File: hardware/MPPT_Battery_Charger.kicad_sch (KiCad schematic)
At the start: 74 parts, among them Q24 SI7414DN-T1-E3, Q25 SI7414DN-T1-E3, Q5 SI7414DN-T1-E3, Q6 SI7414DN-T1-E3, Q8 SI2302DDS-T1-GE3, U22 BQ24650RVAT, U26 LMV321RIYLT, U28 LMV321RIYLT, U4 INA199C1DCKR

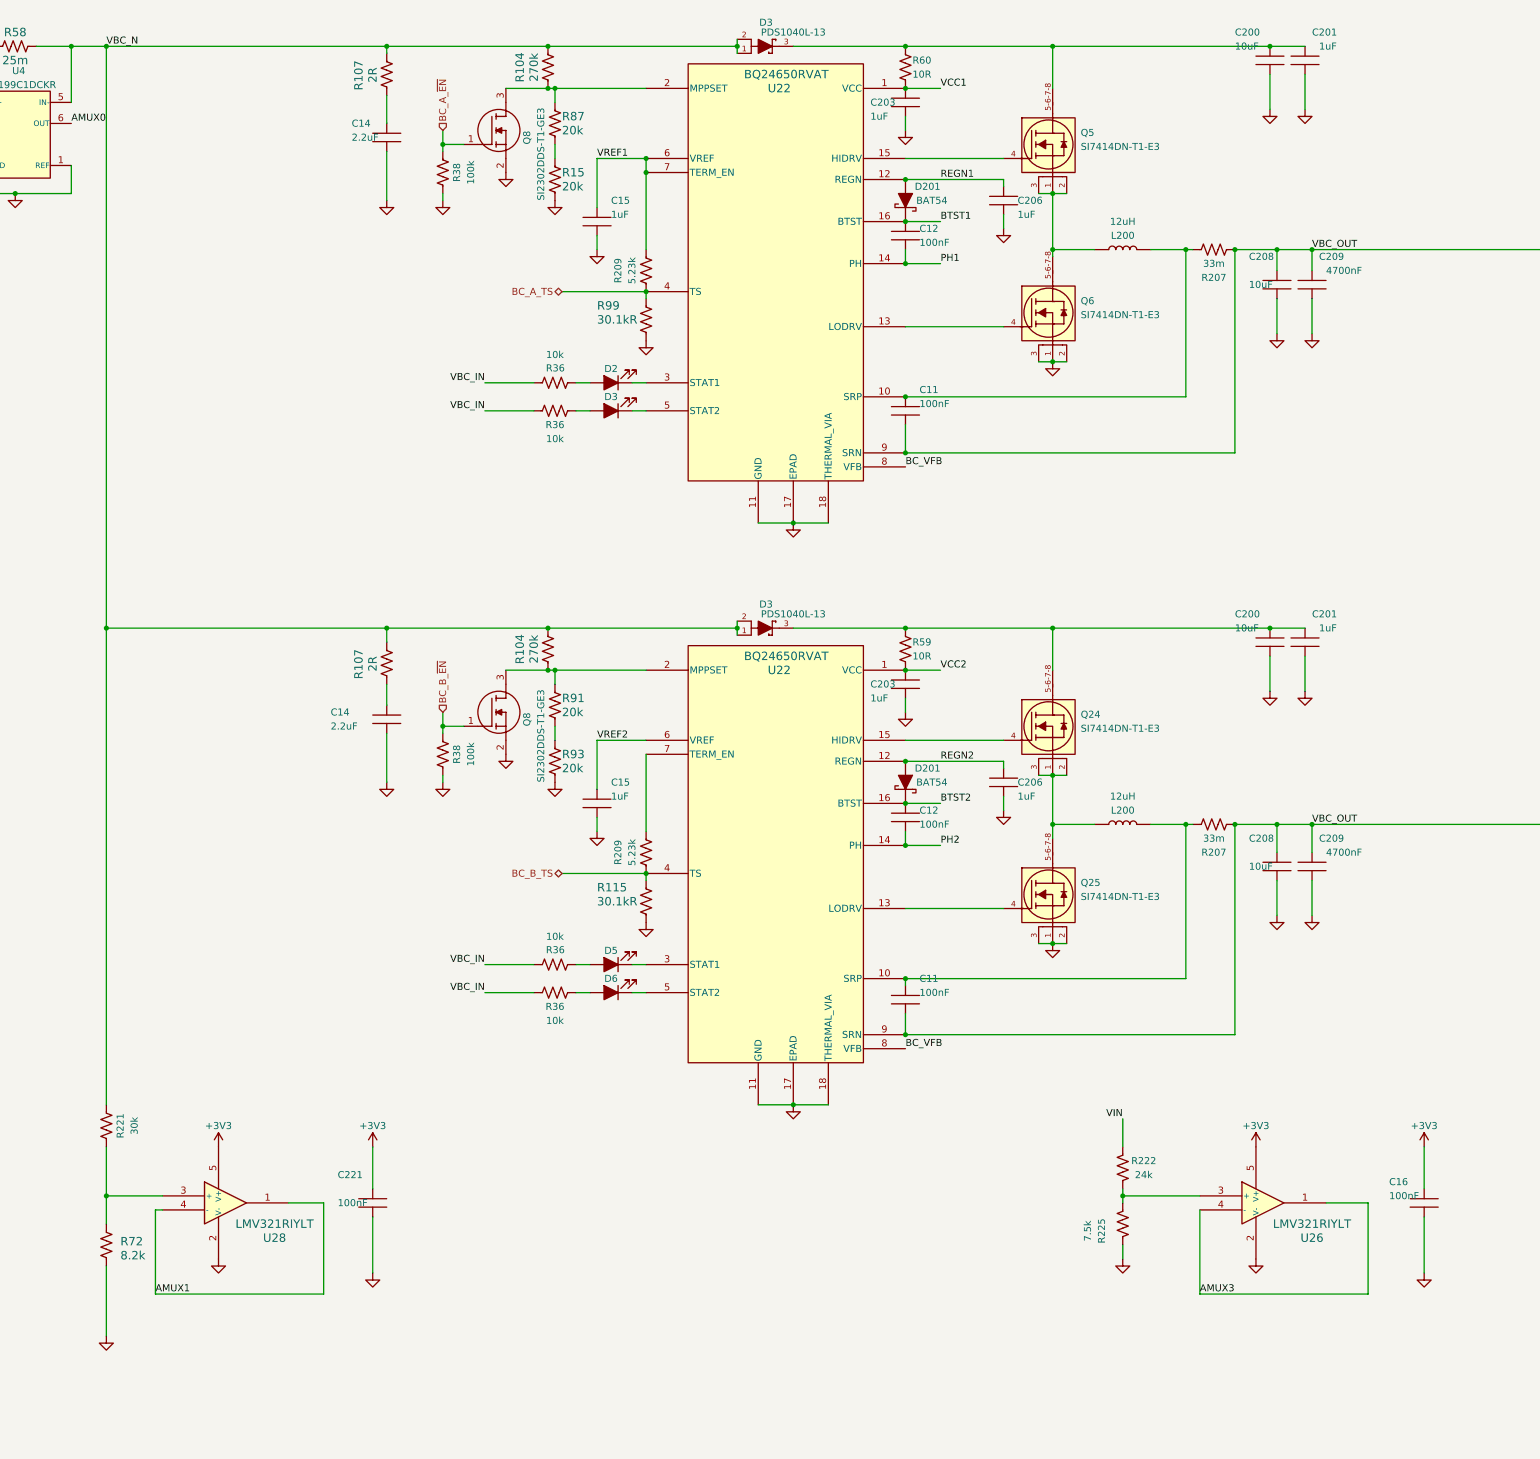
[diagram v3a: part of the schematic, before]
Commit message: hardware: Updating the schematic considering issues #2, #3, #4, #5 and #6.
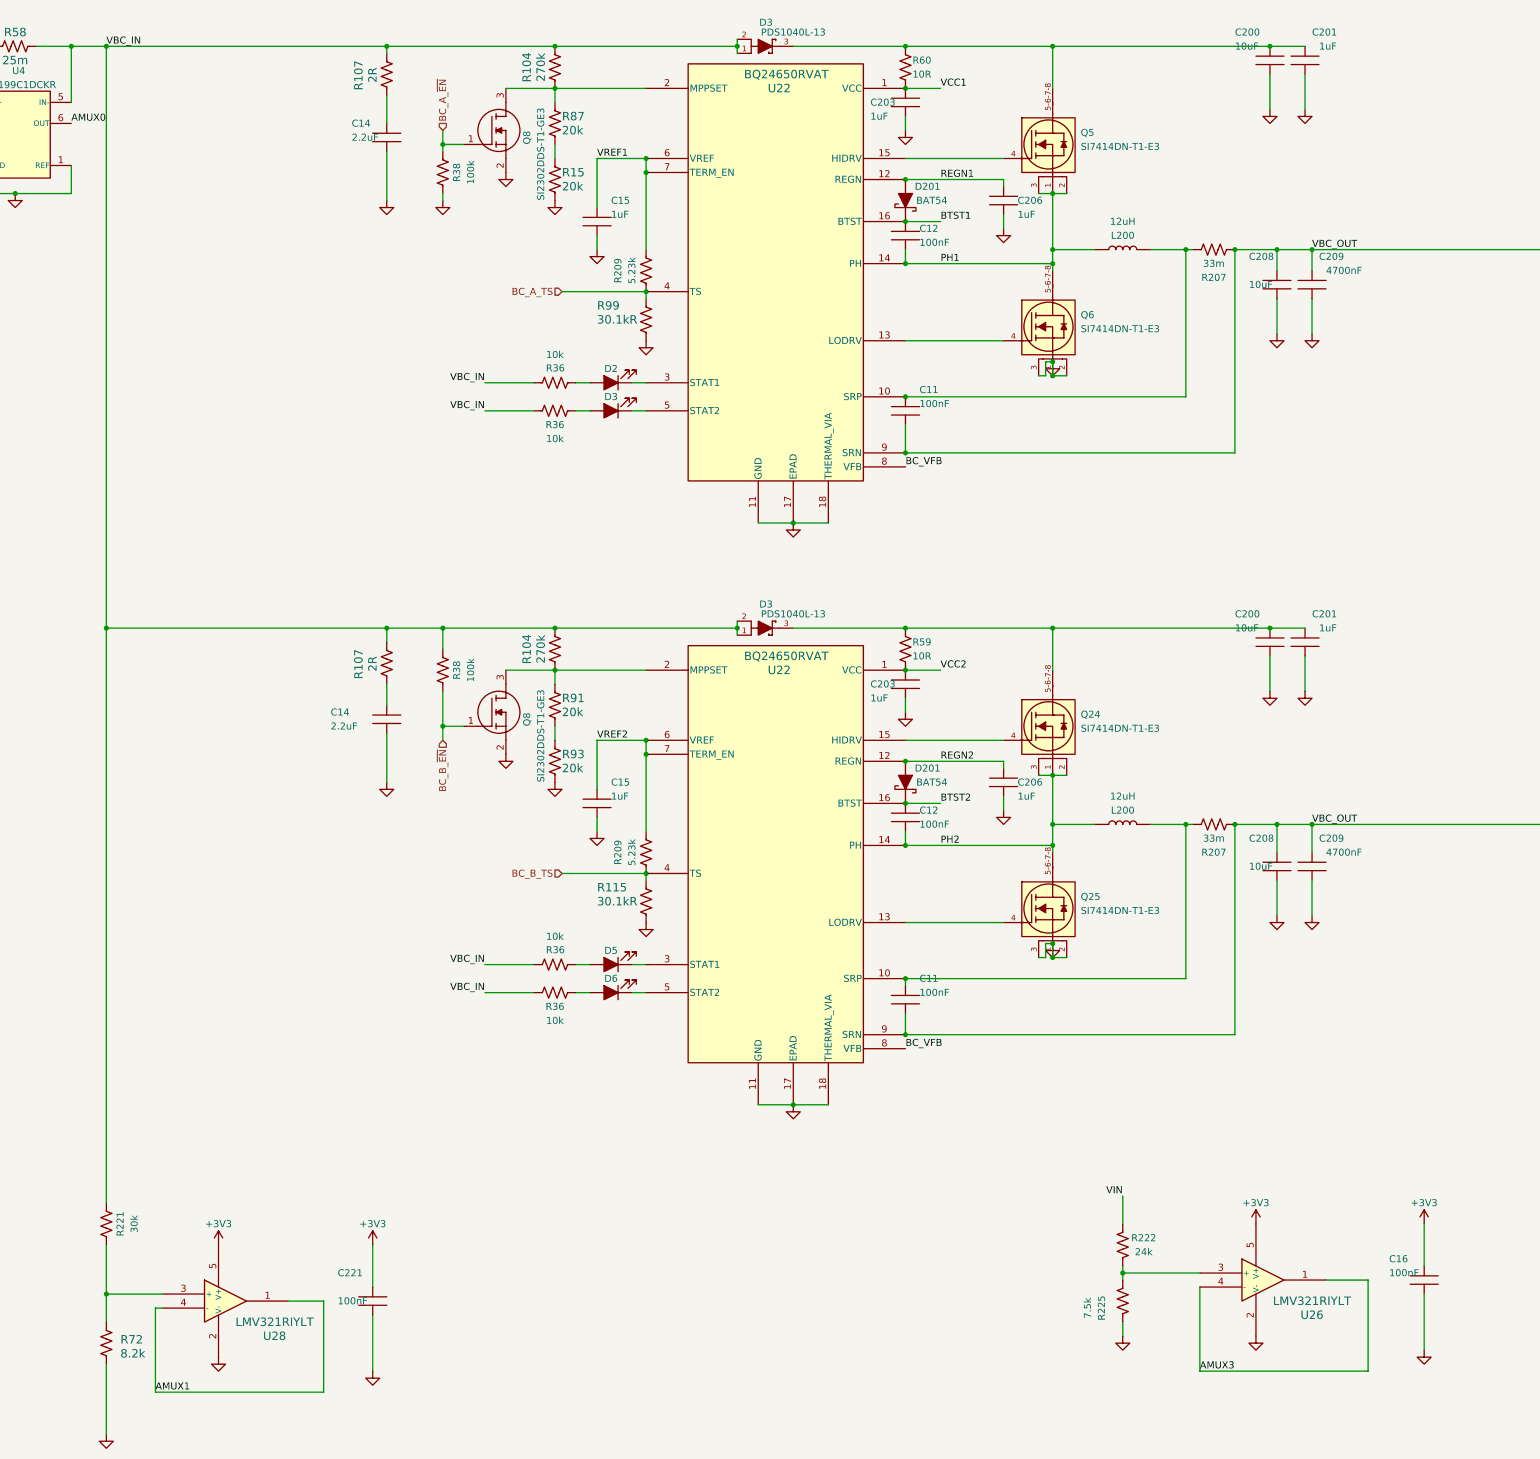
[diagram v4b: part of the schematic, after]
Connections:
- net VBC_N is gone; now on net VBC_IN: D3.1, D3.1, D3.2, D3.2, R104.2, R104.2, R107.2, R107.2, R221.2, R58.1, U4.5 (IN-)
- net BC_B_~{EN}: now also R38.1; no longer R38.2
- net GND: no longer R38.1
- net PH1: now also L200.1, Q5.1 (S), Q5.2 (S), Q5.3 (S), Q6.5-6-7-8 (D)
- net PH2: now also L200.1, Q24.1 (S), Q24.2 (S), Q24.3 (S), Q25.5-6-7-8 (D)
- net VBC_IN: now also R38.2
- net VREF2: now also R209.2, U22.7 (TERM_EN)
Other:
- moved on the sheet: C16, C221, Q25, Q6, R104, R221, R222, R225, R38, R72, U26, U28

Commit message: hardware: Updating 3D models, component placement and more.
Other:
- title: (none) -> Reliability Enhanced Electrical Power System
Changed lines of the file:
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@@
 (kicad_sch (version 20230121) (generator eeschema)
   (paper "A3")
+  (title_block
+    (title "Reliability Enhanced Electrical Power System")
+    (date "2023-08-03")
+    (rev "v0.0")
+    (comment 1 "João C. E. Barcellos <joaoclaudiobarcellos@gmail.com>")
+    (comment 2 "Laura Debastiani <laudebastiani@gmail.com>")
+  )
   (junction (at 196.85 137.16) (diameter 0) (color 0 0 0 0)
   )

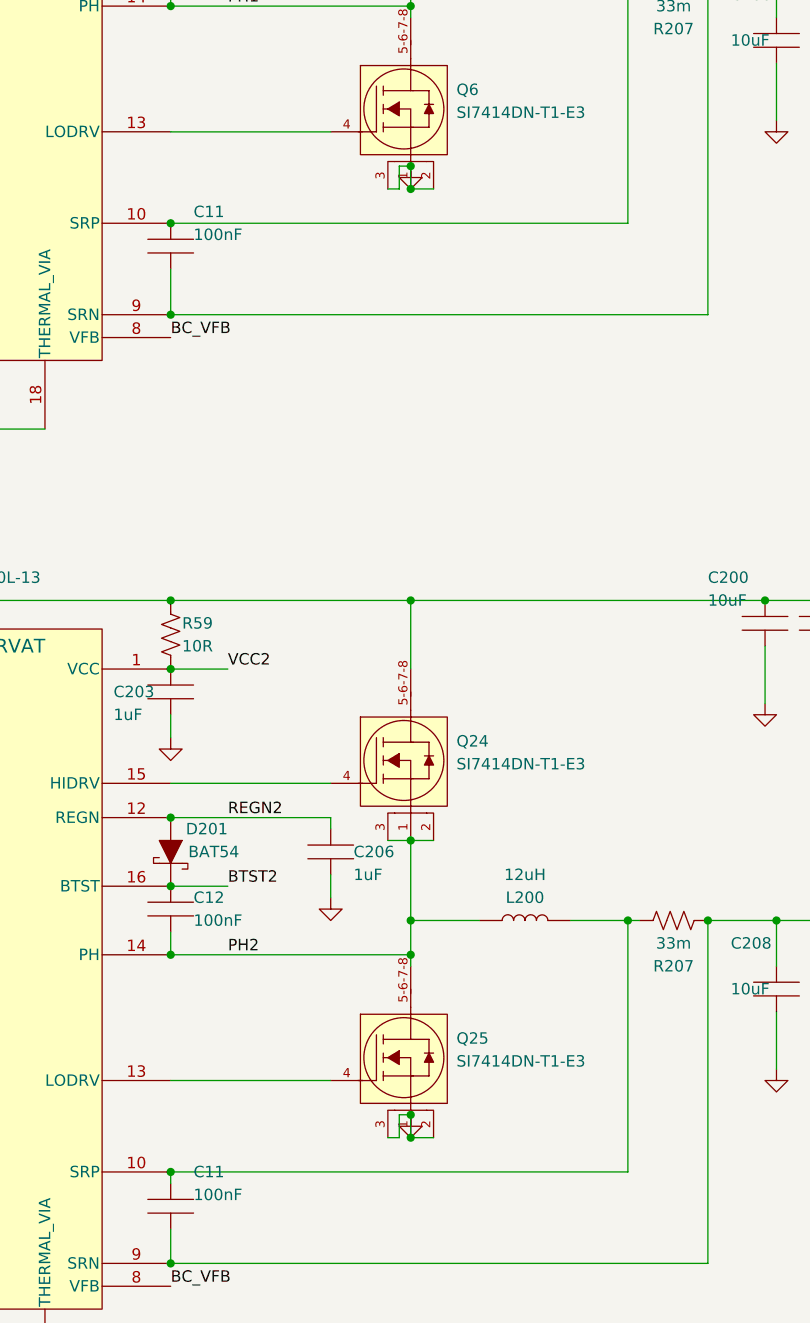
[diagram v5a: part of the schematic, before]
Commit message: hardware: Adding some 3D models, changing the placement of components and routing more nets.
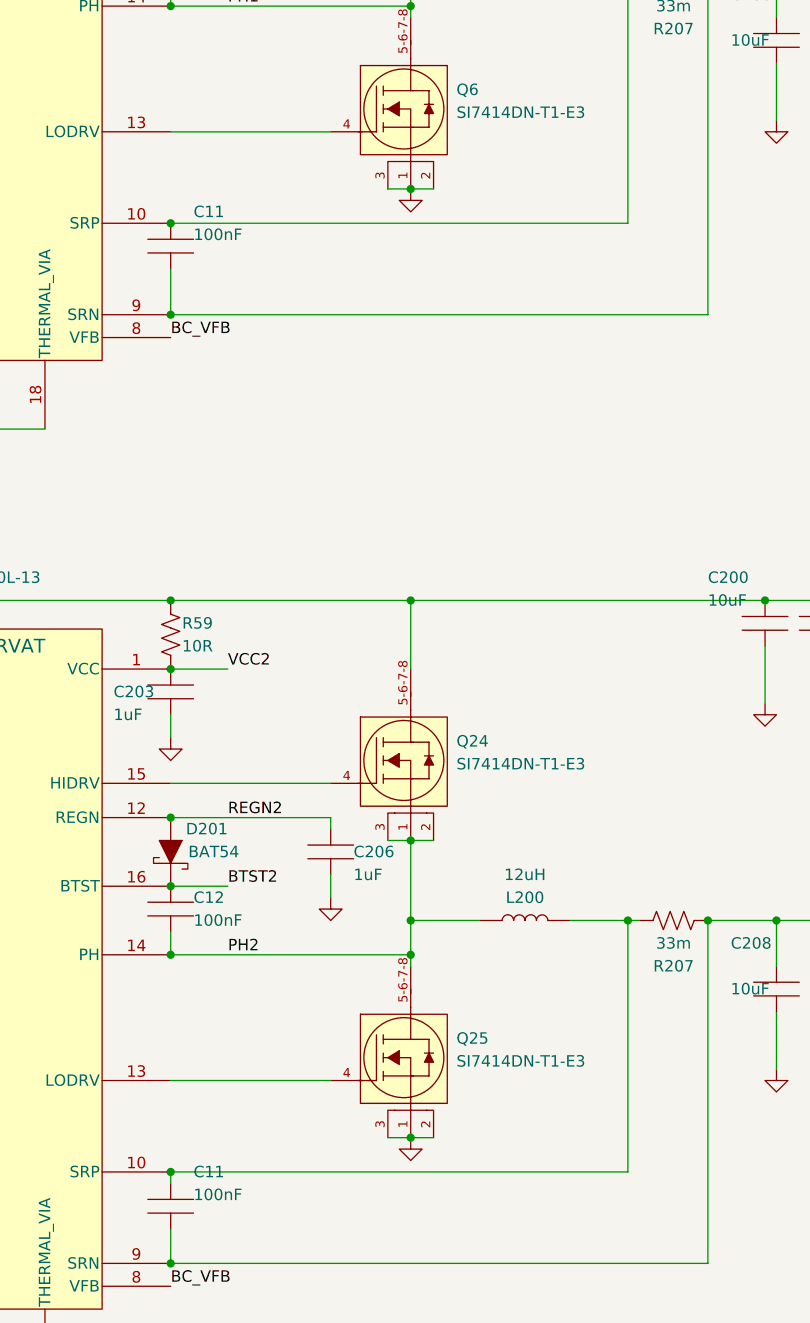
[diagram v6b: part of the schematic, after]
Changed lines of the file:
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@@
   (junction (at 196.85 129.54) (diameter 0) (color 0 0 0 0)
   )
+  (junction (at 223.52 189.23) (diameter 0) (color 0 0 0 0)
+  )
   (junction (at 369.57 87.63) (diameter 0) (color 0 0 0 0)
   )
@@
   (junction (at 45.72 24.13) (diameter 0) (color 0 0 0 0)
   )
-  (junction (at 223.52 186.69) (diameter 0) (color 0 0 0 0)
-  )
   (junction (at 270.51 165.1) (diameter 0) (color 0 0 0 0)
   )
@@
   (junction (at 196.85 203.2) (diameter 0) (color 0 0 0 0)
   )
-  (junction (at 223.52 189.23) (diameter 0) (color 0 0 0 0)
-  )
   (junction (at 360.68 71.12) (diameter 0) (color 0 0 0 0)
   )
@@
   (junction (at 52.07 129.54) (diameter 0) (color 0 0 0 0)
   )
-  (junction (at 312.42 60.96) (diameter 0) (color 0 0 0 0)
+  (junction (at 223.52 83.82) (diameter 0) (color 0 0 0 0)
   )
-  (junction (at 223.52 81.28) (diameter 0) (color 0 0 0 0)
+  (junction (at 312.42 60.96) (diameter 0) (color 0 0 0 0)
   )
   (junction (at 223.52 50.8) (diameter 0) (color 0 0 0 0)
@@
   (junction (at 223.52 129.54) (diameter 0) (color 0 0 0 0)
   )
-  (junction (at 223.52 83.82) (diameter 0) (color 0 0 0 0)
-  )
   (junction (at 113.03 129.54) (diameter 0) (color 0 0 0 0)
   )
@@
     (stroke (width 0) (type default))
   )
-  (wire (pts (xy 222.25 81.28) (xy 223.52 81.28))
-    (stroke (width 0) (type default))
-  )
   (wire (pts (xy 220.98 50.8) (xy 223.52 50.8))
     (stroke (width 0) (type default))
@@
     (stroke (width 0) (type default))
   )
-  (wire (pts (xy 220.98 83.82) (xy 222.25 83.82))
-    (stroke (width 0) (type default))
-  )
   (wire (pts (xy 133.35 137.16) (xy 149.86 137.16))
     (stroke (width 0) (type default))
@@
     (stroke (width 0) (type default))
   )
-  (wire (pts (xy 223.52 83.82) (xy 226.06 83.82))
-    (stroke (width 0) (type default))
-  )
   (wire (pts (xy 269.24 29.21) (xy 269.24 35.56))
     (stroke (width 0) (type default))
@@
     (stroke (width 0) (type default))
   )
-  (wire (pts (xy 220.98 189.23) (xy 222.25 189.23))
-    (stroke (width 0) (type default))
-  )
   (wire (pts (xy 52.07 129.54) (xy 102.87 129.54))
     (stroke (width 0) (type default))
@@
     (stroke (width 0) (type default))
   )
+  (wire (pts (xy 223.52 83.82) (xy 226.06 83.82))
+    (stroke (width 0) (type default))
+  )
   (wire (pts (xy 52.07 250.19) (xy 52.07 255.27))
     (stroke (width 0) (type default))
   )
+  (wire (pts (xy 220.98 189.23) (xy 223.52 189.23))
+    (stroke (width 0) (type default))
+  )
   (wire (pts (xy 223.52 24.13) (xy 223.52 31.75))
     (stroke (width 0) (type default))
@@
     (stroke (width 0) (type default))
   )
-  (wire (pts (xy 223.52 189.23) (xy 223.52 186.69))
-    (stroke (width 0) (type default))
-  )
   (wire (pts (xy 360.68 40.64) (xy 370.84 40.64))
     (stroke (width 0) (type default))
@@
     (stroke (width 0) (type default))
   )
+  (wire (pts (xy 220.98 83.82) (xy 223.52 83.82))
+    (stroke (width 0) (type default))
+  )
   (wire (pts (xy 149.86 152.4) (xy 149.86 166.37))
     (stroke (width 0) (type default))
@@
     (stroke (width 0) (type default))
   )
-  (wire (pts (xy 222.25 83.82) (xy 222.25 81.28))
-    (stroke (width 0) (type default))
-  )
   (wire (pts (xy 360.68 35.56) (xy 370.84 35.56))
     (stroke (width 0) (type default))
@@
     (stroke (width 0) (type default))
   )
-  (wire (pts (xy 223.52 189.23) (xy 226.06 189.23))
-    (stroke (width 0) (type default))
-  )
   (wire (pts (xy 149.86 44.45) (xy 149.86 46.99))
     (stroke (width 0) (type default))
@@
     (stroke (width 0) (type default))
   )
-  (wire (pts (xy 222.25 186.69) (xy 223.52 186.69))
-    (stroke (width 0) (type default))
-  )
   (wire (pts (xy 223.52 168.91) (xy 223.52 170.18))
     (stroke (width 0) (type default))
@@
     (stroke (width 0) (type default))
   )
-  (wire (pts (xy 222.25 189.23) (xy 222.25 186.69))
-    (stroke (width 0) (type default))
-  )
   (wire (pts (xy 196.85 63.5) (xy 223.52 63.5))
     (stroke (width 0) (type default))
@@
     (stroke (width 0) (type default))
   )
+  (wire (pts (xy 223.52 189.23) (xy 226.06 189.23))
+    (stroke (width 0) (type default))
+  )
   (wire (pts (xy 214.63 160.02) (xy 214.63 162.56))
     (stroke (width 0) (type default))
@@
     (stroke (width 0) (type default))
   )
-  (wire (pts (xy 223.52 83.82) (xy 223.52 81.28))
-    (stroke (width 0) (type default))
-  )
   (wire (pts (xy 312.42 165.1) (xy 312.42 60.96))
     (stroke (width 0) (type default))
@@
     )
   )
-  (symbol (lib_id "power:GND") (at 223.52 186.69 0) (unit 1)
+  (symbol (lib_id "power:GND") (at 223.52 189.23 0) (unit 1)
     (in_bom yes) (on_board yes) (dnp no) (fields_autoplaced)
-    (property "Reference" "#PWR057" (at 223.52 193.04 0)
+    (property "Reference" "#PWR057" (at 223.52 195.58 0)
       (effects (font (size 1.27 1.27)) hide)
     )
-    (property "Value" "Earth" (at 223.52 190.5 0)
+    (property "Value" "Earth" (at 223.52 193.04 0)
       (effects (font (size 1.27 1.27)) hide)
     )
-    (property "Footprint" "" (at 223.52 186.69 0)
+    (property "Footprint" "" (at 223.52 189.23 0)
       (effects (font (size 1.27 1.27)) hide)
     )
-    (property "Datasheet" "~" (at 223.52 186.69 0)
+    (property "Datasheet" "~" (at 223.52 189.23 0)
       (effects (font (size 1.27 1.27)) hide)
     )
@@
     )
   )
-  (symbol (lib_id "power:GND") (at 223.52 81.28 0) (unit 1)
+  (symbol (lib_id "power:GND") (at 223.52 83.82 0) (unit 1)
     (in_bom yes) (on_board yes) (dnp no) (fields_autoplaced)
-    (property "Reference" "#PWR057" (at 223.52 87.63 0)
+    (property "Reference" "#PWR057" (at 223.52 90.17 0)
       (effects (font (size 1.27 1.27)) hide)
     )
-    (property "Value" "Earth" (at 223.52 85.09 0)
+    (property "Value" "Earth" (at 223.52 87.63 0)
       (effects (font (size 1.27 1.27)) hide)
     )
-    (property "Footprint" "" (at 223.52 81.28 0)
+    (property "Footprint" "" (at 223.52 83.82 0)
       (effects (font (size 1.27 1.27)) hide)
     )
-    (property "Datasheet" "~" (at 223.52 81.28 0)
+    (property "Datasheet" "~" (at 223.52 83.82 0)
       (effects (font (size 1.27 1.27)) hide)
     )
